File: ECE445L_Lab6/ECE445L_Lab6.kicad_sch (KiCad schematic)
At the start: 32 parts, among them J1 JTAG, J2 Battery, SW1 Reset, SW2 Input, U1 TM4C123GH6PMIR, U2 Adafruit ST7735R, U3 LP2950-33LPRE3, Y1 ABM3-16.000MHZ-B2-T

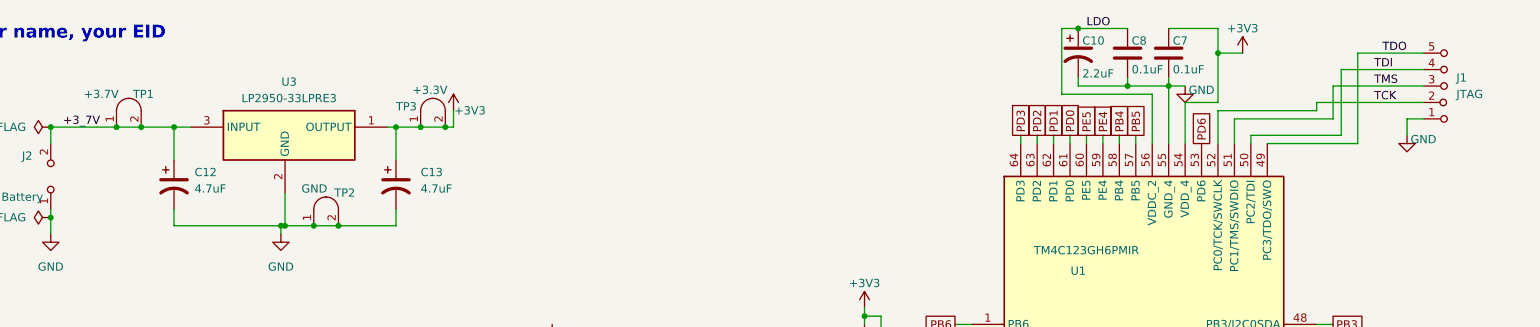
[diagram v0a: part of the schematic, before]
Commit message: Swap TDI and TDO
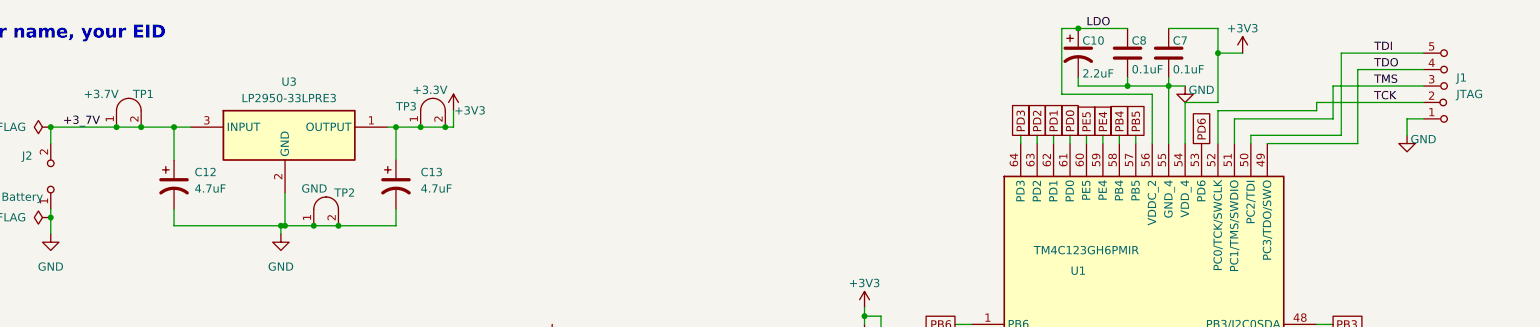
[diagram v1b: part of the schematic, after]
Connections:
- net TDI: now also J1.5 (C); no longer J1.4 (C)
- net TDO: now also J1.4 (C); no longer J1.5 (C)
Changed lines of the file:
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@@
 (kicad_sch
-	(version 20231120)
+	(version 20250114)
 	(generator "eeschema")
-	(generator_version "8.0")
+	(generator_version "9.0")
 	(paper "A4")
 	(title_block
@@
 		(company "The University of Texas at Austin")
 	)
+	(text "Your name, your EID"
+		(exclude_from_sim no)
+		(at 13.97 15.875 0)
+		(effects
+			(font
+				(size 2 2)
+				(thickness 0.6)
+				(bold yes)
+			)
+			(justify left bottom)
+		)
+	)
 	(junction
 		(at 200.66 22.86)
@@
 	(wire
 		(pts
-			(xy 227.33 30.48) (xy 227.33 20.32)
-		)
-		(stroke
-			(width 0)
-			(type default)
-		)
-	)
-	(wire
-		(pts
 			(xy 223.52 72.39) (xy 226.06 72.39)
 		)
@@
 	(wire
 		(pts
-			(xy 229.87 31.75) (xy 229.87 17.78)
-		)
-		(stroke
-			(width 0)
-			(type default)
-		)
-	)
-	(wire
-		(pts
 			(xy 167.64 92.71) (xy 170.18 92.71)
 		)
@@
 	(wire
 		(pts
-			(xy 229.87 17.78) (xy 240.03 17.78)
-		)
-		(stroke
-			(width 0)
-			(type default)
-		)
-	)
-	(wire
-		(pts
 			(xy 167.64 95.25) (xy 170.18 95.25)
 		)
@@
 	(wire
 		(pts
+			(xy 229.87 31.75) (xy 229.87 20.32)
+		)
+		(stroke
+			(width 0)
+			(type default)
+		)
+	)
+	(wire
+		(pts
 			(xy 153.67 58.42) (xy 153.67 59.69)
 		)
@@
 	(wire
 		(pts
+			(xy 229.87 20.32) (xy 240.03 20.32)
+		)
+		(stroke
+			(width 0)
+			(type default)
+		)
+	)
+	(wire
+		(pts
 			(xy 186.69 22.86) (xy 194.31 22.86)
 		)
@@
 	(wire
 		(pts
-			(xy 227.33 20.32) (xy 240.03 20.32)
+			(xy 193.04 123.19) (xy 193.04 127)
 		)
 		(stroke
@@
 	(wire
 		(pts
-			(xy 193.04 123.19) (xy 193.04 127)
+			(xy 153.67 57.15) (xy 153.67 58.42)
 		)
 		(stroke
@@
 	(wire
 		(pts
-			(xy 153.67 57.15) (xy 153.67 58.42)
+			(xy 240.03 27.94) (xy 237.49 27.94)
 		)
 		(stroke
@@
 	(wire
 		(pts
-			(xy 240.03 27.94) (xy 237.49 27.94)
+			(xy 167.64 69.85) (xy 170.18 69.85)
 		)
 		(stroke
@@
 	(wire
 		(pts
-			(xy 167.64 69.85) (xy 170.18 69.85)
+			(xy 227.33 17.78) (xy 240.03 17.78)
 		)
 		(stroke
@@
 	(wire
 		(pts
+			(xy 227.33 17.78) (xy 227.33 30.48)
+		)
+		(stroke
+			(width 0)
+			(type default)
+		)
+	)
+	(wire
+		(pts
 			(xy 81.28 29.21) (xy 81.28 34.29)
 		)
@@
 		)
 	)
-	(text "Your name, your EID"
-		(exclude_from_sim no)
-		(at 13.97 15.875 0)
-		(effects
-			(font
-				(size 2 2)
-				(thickness 0.6)
-				(bold yes)
-			)
-			(justify left bottom)
-		)
-	)
 	(label "OSC2"
 		(at 232.41 83.82 0)
@@
 		)
 	)
-	(label "TCK"
-		(at 232.41 25.4 0)
+	(label "TDO"
+		(at 232.41 20.32 0)
 		(effects
 			(font
@@
 		)
 	)
-	(label "TDI"
-		(at 232.41 20.32 0)
+	(label "TCK"
+		(at 232.41 25.4 0)
 		(effects
 			(font
@@
 		)
 	)
-	(label "TDO"
-		(at 233.68 17.78 0)
-		(effects
-			(font
-				(size 1.27 1.27)
-			)
-			(justify left bottom)
-		)
-	)
 	(label "TMS"
 		(at 232.41 22.86 0)
@@
 		)
 	)
+	(label "TDI"
+		(at 232.41 17.78 0)
+		(effects
+			(font
+				(size 1.27 1.27)
+			)
+			(justify left bottom)
+		)
+	)
 	(global_label "PD7"
 		(shape passive)
@@
 		)
 	)
+	(embedded_fonts no)
 )

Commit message: update all symbols and re-sync footprints in the KiCad projects
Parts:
- U3: footprint ECE445L:TL431CLPM -> Package_TO_SOT_THT:TO-92_Inline_Wide
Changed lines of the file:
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@@
 			)
 		)
-		(property "Footprint" "ECE445L:TL431CLPM"
+		(property "Footprint" "Package_TO_SOT_THT:TO-92_Inline_Wide"
 			(at 76.2 124.13 0)
 			(effects
